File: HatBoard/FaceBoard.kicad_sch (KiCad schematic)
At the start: 18 parts, among them J1 Molex FC Connection, J2 DF11 FC Connection, J3 Conn_01x04, U1 VEML7700, U2 DRV2605LDGS, U3 MCP9808_DFN, U4 TCA4311A

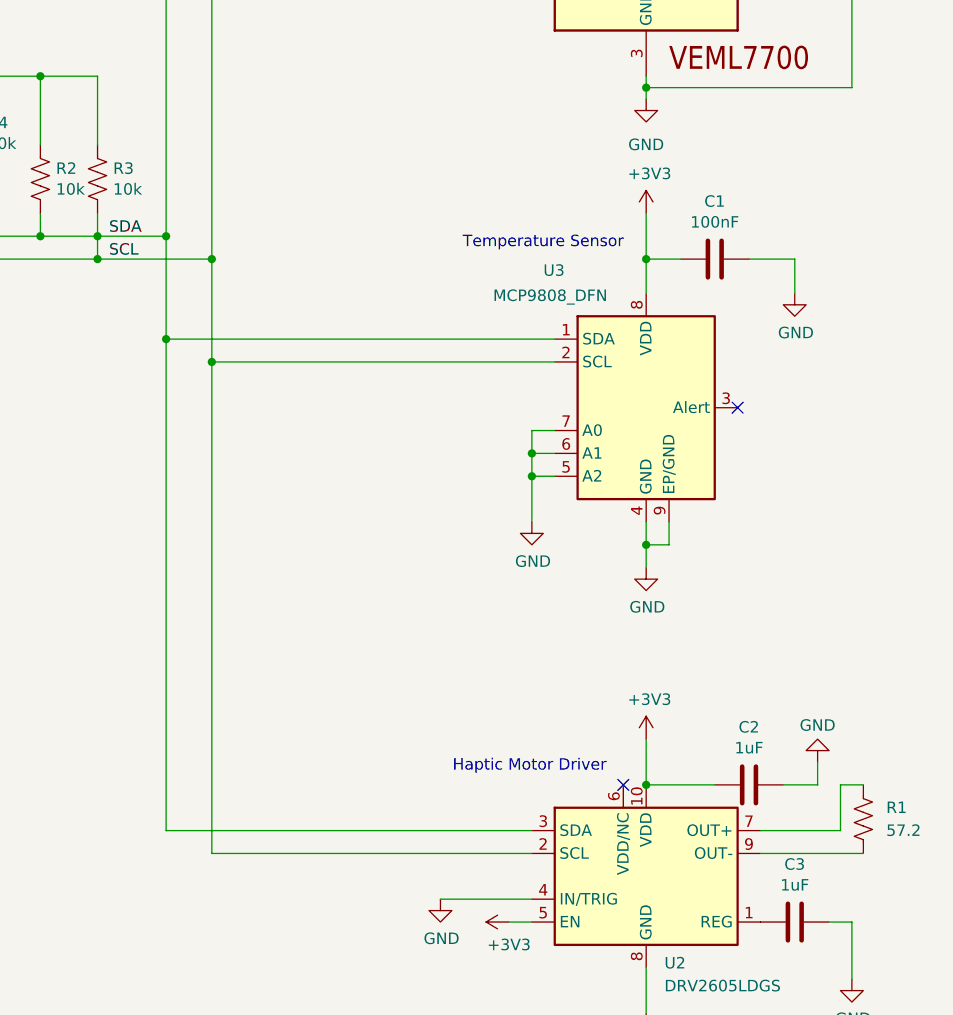
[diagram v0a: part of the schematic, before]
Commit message: placement with new temp sensor
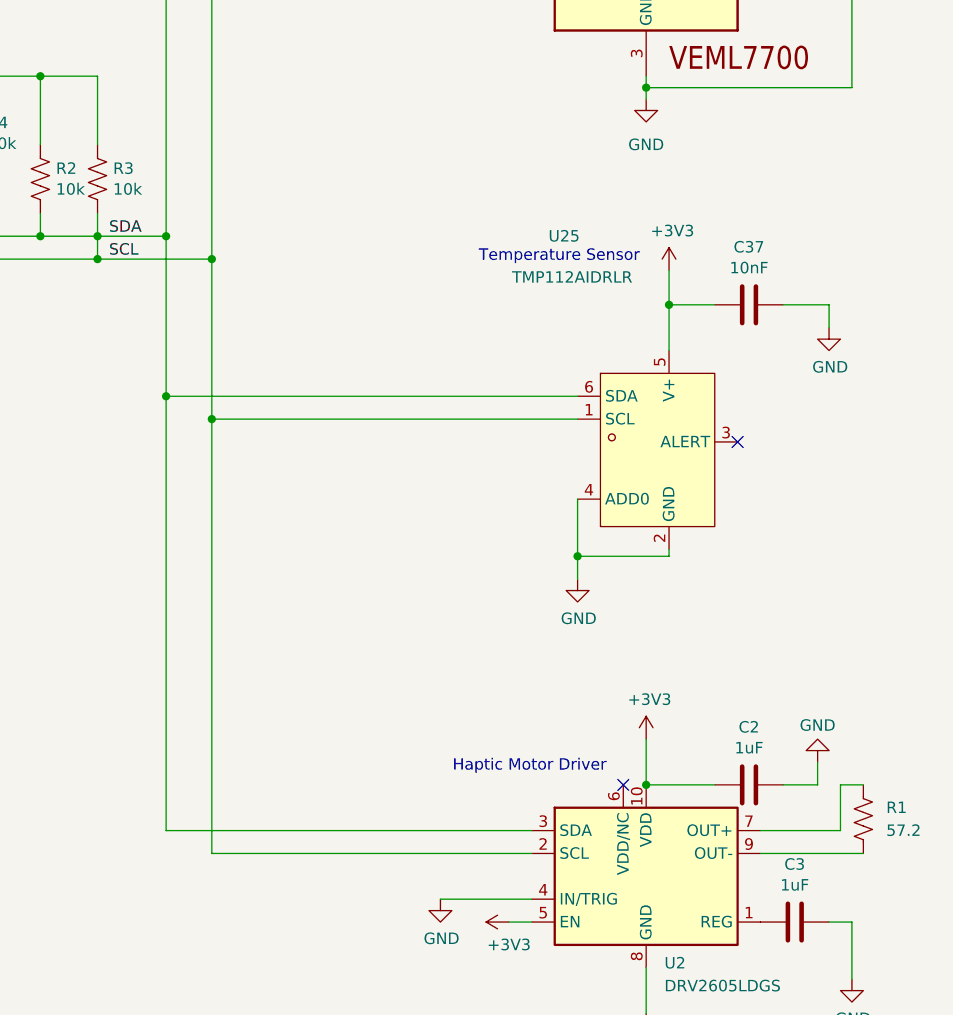
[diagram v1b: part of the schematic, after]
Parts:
- removed C1: 100nF, Capacitor_SMD:C_0402_1005Metric, symbol Device:C
- removed U3: MCP9808_DFN, easyeda2kicad:MSOP-8_L3.0-W3.0-P0.65-LS4.9-BL, symbol Sensor_Temperature:MCP9808_DFN
- added C37: 10nF, Capacitor_SMD:C_0402_1005Metric, symbol Device:C
- added U25: TMP112AIDRLR, easyeda2kicad:SOT-563_L1.6-W1.2-P0.50-LS1.6-BR, symbol easyeda2kicad:TMP112AIDRLR
- J3: footprint (none) -> Connector_PinHeader_2.00mm:PinHeader_1x04_P2.00mm_Vertical
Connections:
- net +3V3: now also C37.1, U25.5 (V+)
- net GND: now also C37.2, U25.2 (GND), U25.4 (ADD0)
- net SCL: now also U25.1 (SCL), U25.6 (SDA)

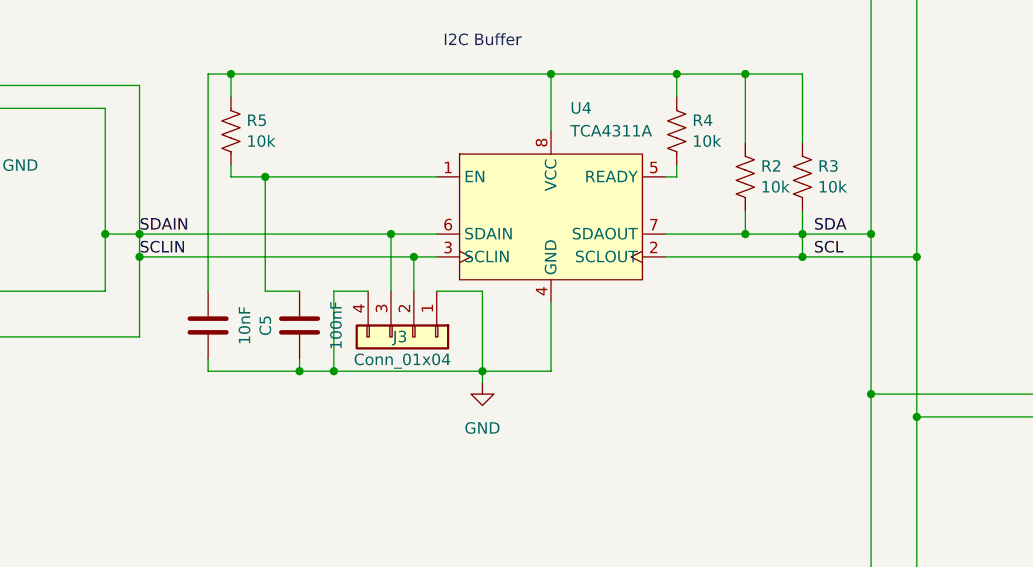
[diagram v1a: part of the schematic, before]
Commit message: no design errors faceboard
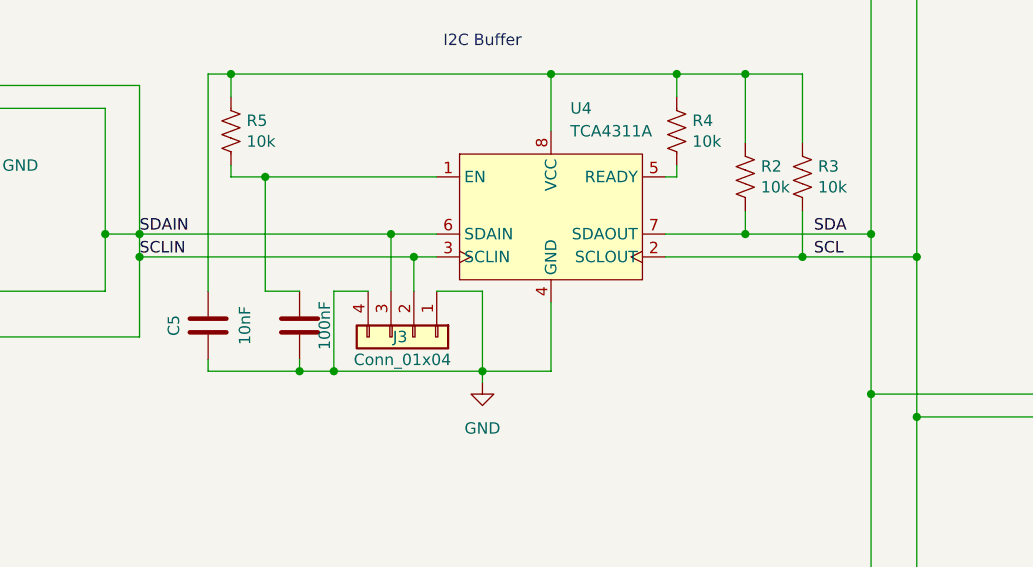
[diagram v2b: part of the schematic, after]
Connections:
- net SCL: no longer R2.2, U1.4 (SDA), U2.3 (SDA), U25.6 (SDA), U4.7 (SDAOUT)
- new net SDA: R2.2, U1.4 (SDA), U2.3 (SDA), U25.6 (SDA), U4.7 (SDAOUT)
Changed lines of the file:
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@@
 	)
 	(junction
-		(at 152.4 69.85)
-		(diameter 0)
-		(color 0 0 0 0)
-	)
-	(junction
 		(at 138.43 52.07)
 		(diameter 0)
@@
 	(wire
 		(pts
-			(xy 146.05 69.85) (xy 152.4 69.85)
+			(xy 146.05 69.85) (xy 160.02 69.85)
 		)
 		(stroke
@@
 	(wire
 		(pts
-			(xy 152.4 69.85) (xy 160.02 69.85)
-		)
-		(stroke
-			(width 0)
-			(type default)
-		)
-	)
-	(wire
-		(pts
 			(xy 57.15 50.8) (xy 45.72 50.8)
 		)
@@
 	(wire
 		(pts
-			(xy 152.4 69.85) (xy 152.4 72.39)
+			(xy 152.4 67.31) (xy 152.4 72.39)
 		)
 		(stroke
@@
 	(wire
 		(pts
-			(xy 152.4 67.31) (xy 152.4 69.85)
-		)
-		(stroke
-			(width 0)
-			(type default)
-		)
-	)
-	(wire
-		(pts
 			(xy 86.36 83.82) (xy 86.36 85.09)
 		)
@@
 		(dnp no)
 		(property "Reference" "C5"
-			(at 92.7608 80.01 90)
+			(at 82.55 80.01 90)
 			(effects
 				(font
@@
 		)
 		(property "Value" "100nF"
-			(at 100.6094 80.01 90)
+			(at 99.314 80.01 90)
 			(effects
 				(font

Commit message: schematic corrections
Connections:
- net +3V3: now also C5.1, J1.5 (Pin_5), J2.5 (Pin_5), R2.1, R3.1, R4.1, R5.1, U4.8 (VCC)
- net GND: now also J1.6 (Pin_6), J2.3 (Pin_3)
- no-connect marks 6 -> 2
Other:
- moved on the sheet: R5

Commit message: new everything should be here
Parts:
- removed C2, C3: 1uF, Capacitor_SMD:C_0805_2012Metric, symbol Device:C
- removed C37: 10nF, Capacitor_SMD:C_0402_1005Metric, symbol Device:C
- removed C6: 100nF, Capacitor_SMD:C_0402_1005Metric, symbol Device:C
- removed J1: Molex FC Connection, easyeda2kicad:CONN-SMD_6P-P1.50_A1501WRB-S-6P, symbol Connector_Generic:Conn_01x06
- removed J2: DF11 FC Connection, Connector_Hirose:Hirose_DF11-6DP-2DSA_2x03_P2.00mm_Vertical, symbol Connector_Generic:Conn_02x03_Odd_Even
- removed J3: Conn_01x04, Connector_PinHeader_2.00mm:PinHeader_1x04_P2.00mm_Vertical, symbol Connector_Generic:Conn_01x04
- removed R1: 57.2, Resistor_SMD:R_0201_0603Metric_Pad0.64x0.40mm_HandSolder, symbol Device:R_US
- removed R2, R3: 10k, Resistor_SMD:R_0603_1608Metric, symbol Device:R_US
- removed U1: VEML7700, easyeda2kicad:SENSOR-SMD_EML7700-TT, symbol Adafruit VEML7700-eagle-import:VEML7700
- removed U2: DRV2605LDGS, Package_SO:VSSOP-10_3x3mm_P0.5mm, symbol Driver_Haptic:DRV2605LDGS
- removed U25: TMP112AIDRLR, easyeda2kicad:SOT-563_L1.6-W1.2-P0.50-LS1.6-BR, symbol easyeda2kicad:TMP112AIDRLR
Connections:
- net SCLIN: no longer U4.6 (SDAIN)
- new net SDAIN: U4.6 (SDAIN)
- no-connect marks 2 -> 0
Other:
- note removed: "Haptic Motor Driver"
- note removed: "Light Sensor"
- note removed: "Temperature Sensor"
- moved on the sheet: C5, R4, R5, U4
